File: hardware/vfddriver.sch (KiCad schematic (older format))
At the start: 8 parts, among them J1 Connection Header, U1 IVL2-5_7, U4 HV5812WG

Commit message: update vfddriver resistor values, 10 ohm is too dark, 4.7 too bright
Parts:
- R14: value 4.7kΩ -> 47kΩ
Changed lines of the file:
@@
 encoding utf-8
 Sheet 1 2
-Title ""
-Date ""
+Title "VFD Driver Board"
+Date "2020-07-22"
 Rev "1"
 Comp ""
 Comment1 "Designed for AISLER 2-Layer Service"
-Comment2 ""
+Comment2 "Driving an IVL2-7/5 Display"
 Comment3 ""
 Comment4 ""
@@
 P 8650 5400
 F 0 "R14" H 8709 5446 50  0000 L CNN
-F 1 "4.7kΩ" H 8709 5355 50  0000 L CNN
+F 1 "47kΩ" H 8709 5355 50  0000 L CNN
 F 2 "Resistor_SMD:R_0805_2012Metric_Pad1.15x1.40mm_HandSolder" H 8650 5400 50  0001 C CNN
 F 3 "~" H 8650 5400 50  0001 C CNN

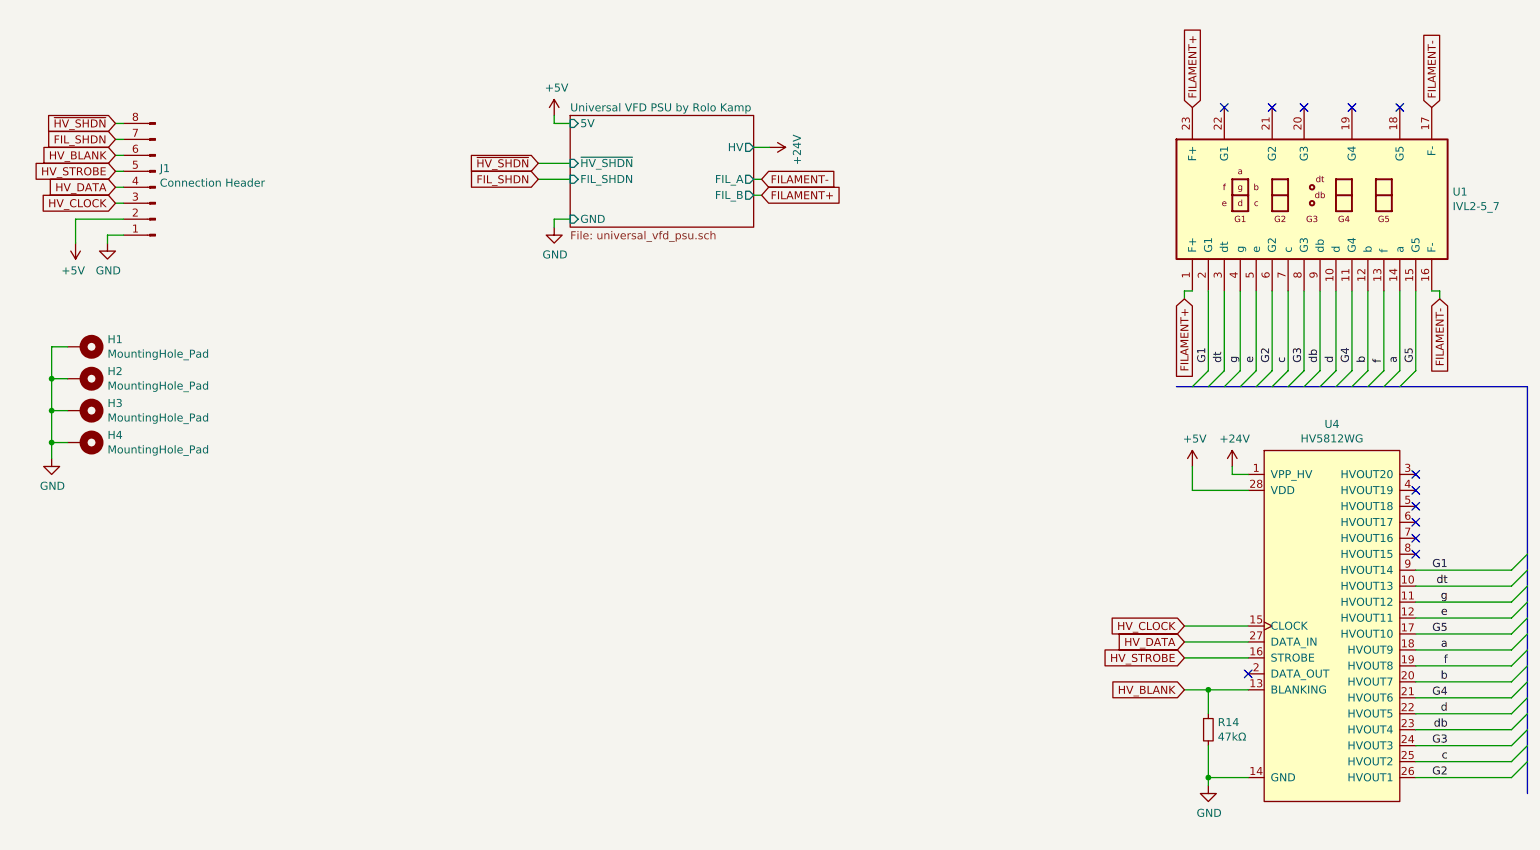
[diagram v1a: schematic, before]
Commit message: hardware: tidy up, fix photodiode, (re)export (i)boms and schematics
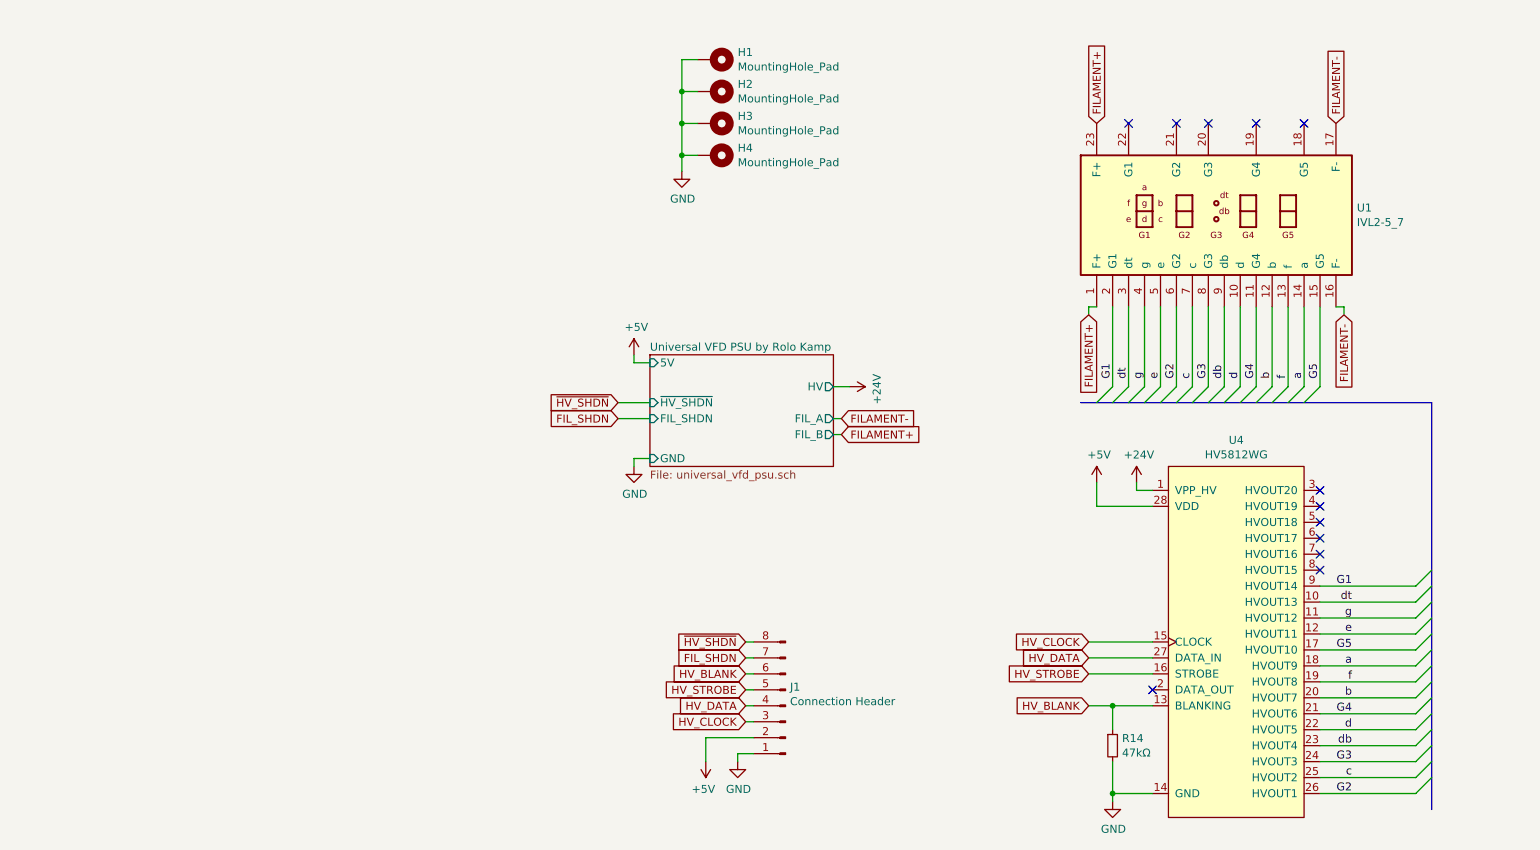
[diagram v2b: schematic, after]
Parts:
- J1: Digi-Key PN (none) -> S2112EC-40-ND; MPN (none) -> PREC040DBAN-M71RC; Mfg (none) -> Sullins
- R14: Digi-Key PN (none) -> 311-47.0KCRCT-ND; MPN (none) -> RC0805FR-0747KL; Mfg (none) -> Yageo
- U1: MPN (none) -> IVL2-7/5
- U4: Digi-Key PN (none) -> HV5812WG-GCT-ND; MPN (none) -> HV5812WG-G; Mfg (none) -> Microchip
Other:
- moved on the sheet: H1, H2, H3, H4, J1, R14, U1, U4

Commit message: hw: [WIP] add attiny412, remove traces in prep for v2
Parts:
- added U5: ATtiny412-SS, Package_SO:SOIC-8_3.9x4.9mm_P1.27mm, symbol MCU_Microchip_ATtiny:ATtiny412-SS
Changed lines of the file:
@@
 S 5150 3050 1150 700
 U 5F189B7D
-F0 "Universal VFD PSU by Rolo Kamp" 50
+F0 "Universal VFD PSU" 50
 F1 "universal_vfd_psu.sch" 50
 F2 "5V" I L 5150 3100 50
@@
 Wire Wire Line
 	6300 3550 6350 3550
-$Comp
-L HV5812:HV5812WG U4
-U 1 1 5F19BBE0
-P 8800 3650
-F 0 "U4" H 8825 3715 50  0000 C CNN
-F 1 "HV5812WG" H 8825 3624 50  0000 C CNN
-F 2 "Package_SO:SOIC-28W_7.5x17.9mm_P1.27mm" H 8800 3650 50  0001 C CNN
-F 3 "http://www.microchip.com/mymicrochip/filehandler.aspx?ddocname=en570713" H 8800 3650 50  0001 C CNN
-F 4 "HV5812WG-GCT-ND" H 8800 3650 50  0001 C CNN "Digi-Key PN"
-F 5 "HV5812WG-G" H 8800 3650 50  0001 C CNN "MPN"
-F 6 "Microchip" H 8800 3650 50  0001 C CNN "Mfg"
-	1    8800 3650
-	1    0    0    -1
-$EndComp
 $Comp
 L power:+24V #PWR0105
@@
 Wire Bus Line
 	7850 3350 10050 3350
+$Comp
+L MCU_Microchip_ATtiny:ATtiny412-SS U5
+U 1 1 612A9264
+P 2300 2050
+F 0 "U5" H 1771 2096 50  0000 R CNN
+F 1 "ATtiny412-SS" H 1771 2005 50  0000 R CNN
+F 2 "Package_SO:SOIC-8_3.9x4.9mm_P1.27mm" H 2300 2050 50  0001 C CIN
+F 3 "http://ww1.microchip.com/downloads/en/DeviceDoc/40001911A.pdf" H 2300 2050 50  0001 C CNN
+	1    2300 2050
+	1    0    0    -1
+$EndComp
+$Comp
+L HV5812:HV5812WG U4
+U 1 1 5F19BBE0
+P 8800 3650
+F 0 "U4" H 8825 3715 50  0000 C CNN
+F 1 "HV5812WG" H 8825 3624 50  0000 C CNN
+F 2 "Package_SO:SOIC-28W_7.5x17.9mm_P1.27mm" H 8800 3650 50  0001 C CNN
+F 3 "http://www.microchip.com/mymicrochip/filehandler.aspx?ddocname=en570713" H 8800 3650 50  0001 C CNN
+F 4 "HV5812WG-GCT-ND" H 8800 3650 50  0001 C CNN "Digi-Key PN"
+F 5 "HV5812WG-G" H 8800 3650 50  0001 C CNN "MPN"
+F 6 "Microchip" H 8800 3650 50  0001 C CNN "Mfg"
+	1    8800 3650
+	1    0    0    -1
+$EndComp
 $EndSCHEMATC
